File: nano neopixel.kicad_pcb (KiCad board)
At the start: 2 copper layers, 35.5 x 48.2 mm, 25 parts

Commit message: completed layout
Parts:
- added C1: 1000u, Capacitor_THT:CP_Radial_D8.0mm_P3.50mm, F.Cu at (130.8, 82.0)
- added D8: Conn_01x03, Connector_PinHeader_2.54mm:PinHeader_1x03_P2.54mm_Vertical, F.Cu at (134.3, 106.3)
- added D9: Conn_01x03, Connector_PinHeader_2.54mm:PinHeader_1x03_P2.54mm_Vertical, F.Cu at (134.3, 108.9)
- added JP7: Jumper_Open, Jumper:SolderJumper-2_P1.3mm_Open_Pad1.0x1.5mm, B.Cu at (118.5, 109.1)
- added JP8: Jumper_Open, Jumper:SolderJumper-2_P1.3mm_Open_Pad1.0x1.5mm, B.Cu at (118.5, 113.5)
- added R7: 470, Resistor_SMD:R_0805_2012Metric, B.Cu at (118.5, 106.9)
- added R8: 470, Resistor_SMD:R_0805_2012Metric, B.Cu at (118.5, 111.3)
- JP1, JP2, JP3, JP4, JP5, JP6, R1, R2, R3, R4, R5, R6: moved to B.Cu
- moved H3 70.6 mm to (105.2, 115.4), turned to 180 degrees
- moved H4 69.6 mm to (105.2, 74.2), turned to 180 degrees
- moved H2 42.0 mm to (134.9, 115.4), turned to 180 degrees
- moved H1 40.4 mm to (134.9, 74.2), turned to 180 degrees
- moved A1 32.2 mm to (110.7, 76.8)
- moved G*** 31.6 mm to (105.5, 86.4), turned to -90 degrees
- moved R6 27.0 mm to (118.5, 102.5)
- moved R5 26.3 mm to (118.5, 98.1)
- moved R3 25.4 mm to (118.5, 89.3)
- moved R4 25.4 mm to (118.5, 93.7)
- moved R2 24.7 mm to (118.5, 84.9)
- moved R1 24.3 mm to (118.5, 80.5)
- moved JP5 13.7 mm to (118.5, 100.3)
- moved JP6 13.6 mm to (118.5, 104.7)
- moved JP4 13.5 mm to (118.5, 95.9)
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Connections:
- net STRIP1 renamed D2
- net STRIP2 renamed D3
- net STRIP3 renamed D4
- net STRIP4 renamed D5
- net STRIP5 renamed D6
- net STRIP6 renamed D7
- A1 pad 11: unconnected-(A1-Pad11) -> D8
- A1 pad 12: unconnected-(A1-Pad12) -> D9
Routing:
- net +5V: track 49.7 -> 33.2 mm
- net Net-(D2-Pad3): track 0.00 -> 16.1 mm
- net Net-(D5-Pad3): track 0.00 -> 13.7 mm
- net Net-(D9-Pad3): track 0.00 -> 13.4 mm
- net Net-(D8-Pad3): track 0.00 -> 12.6 mm
- net D9: track 0.00 -> 11.9 mm
- net Net-(D3-Pad3): track 3.86 -> 15.5 mm
- net D8: track 0.00 -> 11.2 mm
- net D3: track 0.00 -> 11.1 mm
- net Net-(D4-Pad3): track 3.54 -> 14.6 mm
- net D7: track 0.00 -> 10.4 mm
- net D4: track 0.00 -> 10.3 mm
- net D6: track 0.00 -> 9.63 mm
- net Net-(D7-Pad3): track 3.87 -> 13.1 mm
- net Net-(D6-Pad3): track 3.76 -> 12.8 mm
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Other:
- board size 35.5 x 48.2 mm -> 37.2 x 48.2 mm
- board text added: "D2"
- board text added: "D3"
- board text added: "D4"
- board text added: "D5"
- board text added: "D6"
- board text added: "D7"
- board text added: "D8"
- board text added: "D9"
- board text added: "JLCJLCJLCJLC"

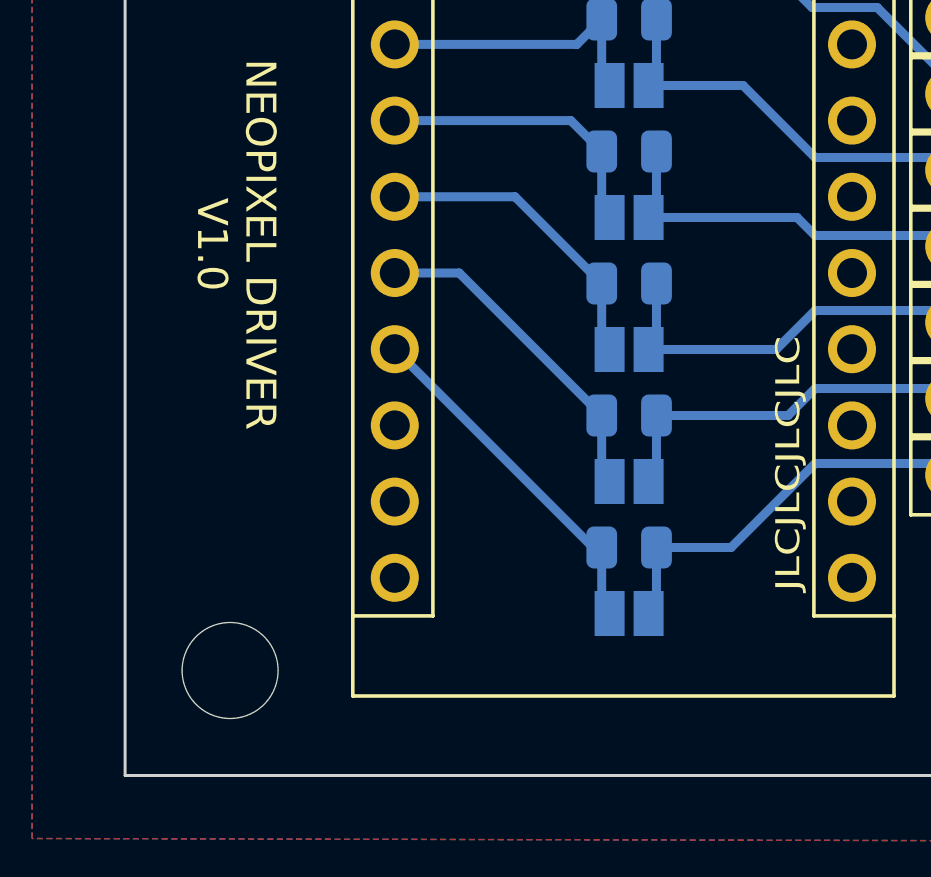
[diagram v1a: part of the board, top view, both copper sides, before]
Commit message: added USB notation to the board
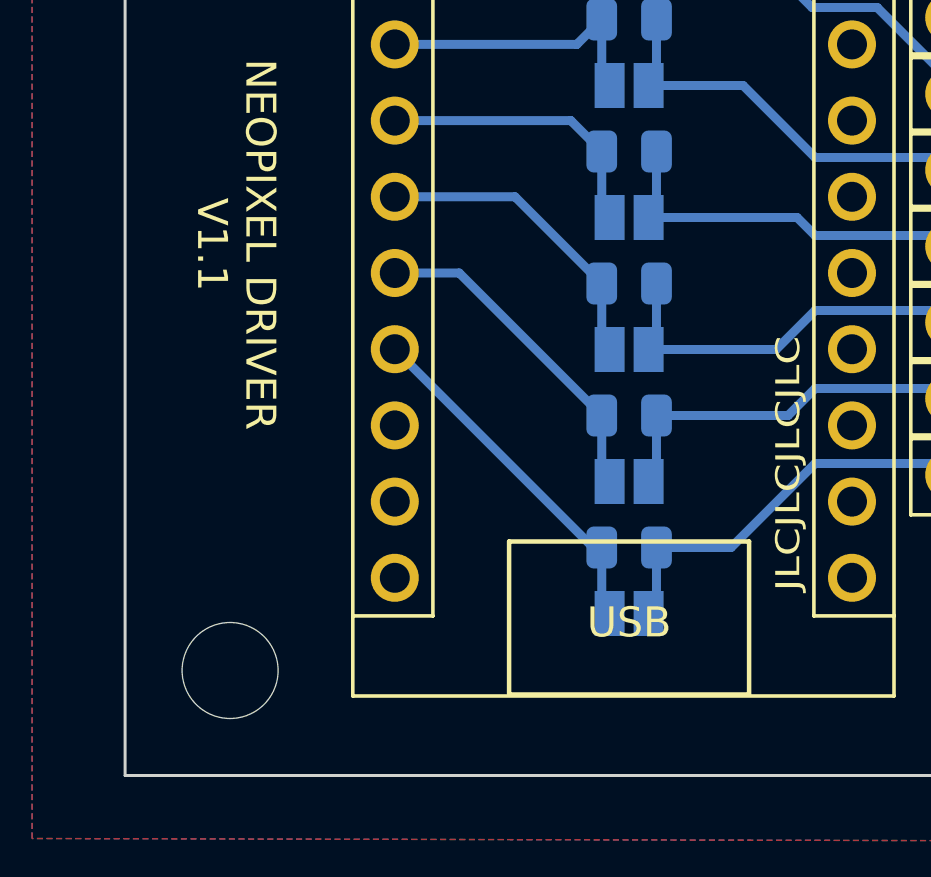
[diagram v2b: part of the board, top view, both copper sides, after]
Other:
- board text added: "NEOPIXEL DRIVER V1.1"
- board text added: "USB"
- board text removed: "NEOPIXEL DRIVER V1.0"
